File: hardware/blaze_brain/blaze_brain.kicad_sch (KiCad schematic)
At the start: 14 parts, among them J1 Conn_01x02, J3 Conn_01x30, J4 Micro_SD_Card, J5 Conn_01x03_Pin, Q2 FDN340P, U3 Teensy4.0, U4 W25N02KVZEIR

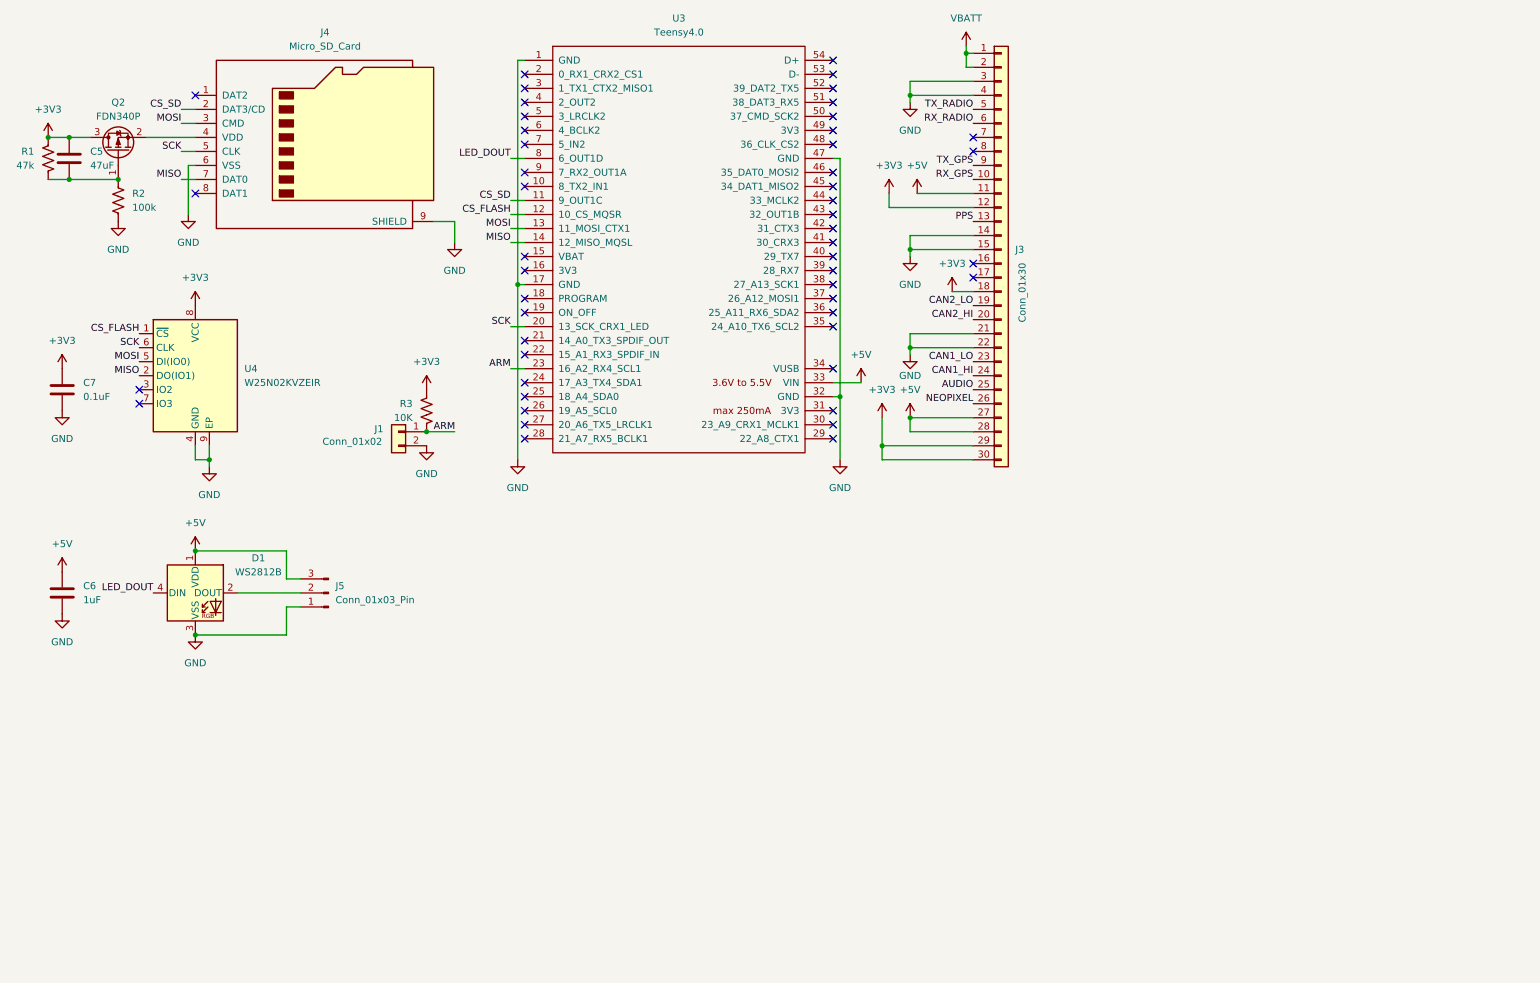
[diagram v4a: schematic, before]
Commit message: Added CAN to Blaze Brain
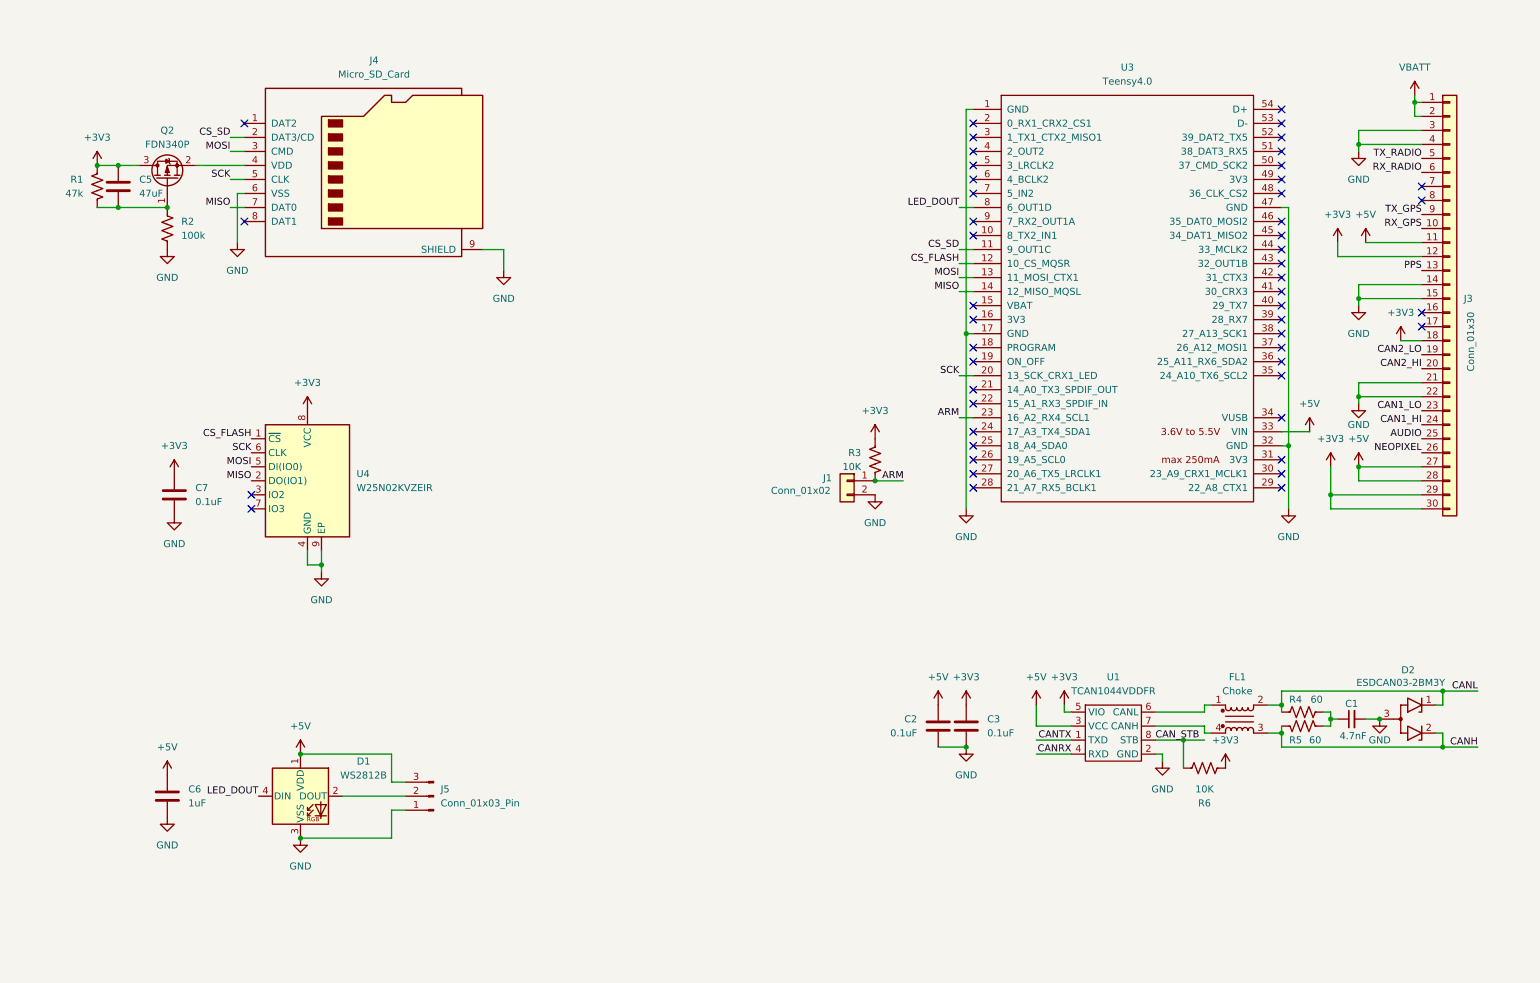
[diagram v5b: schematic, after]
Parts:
- added C1: 4.7nF, symbol Device:C_Small
- added C2, C3: 0.1uF, symbol Device:C
- added D2: ESDCAN03-2BM3Y, Package_TO_SOT_SMD:SOT-416, symbol Power_Protection:RCLAMP0582B
- added FL1: Choke, Inductor_SMD:L_CommonModeChoke_Coilcraft_0603USB, symbol Filter:Choke_Coilcraft_0603USB-142
- added R4, R5: 60, symbol Device:R_US
- added R6: 10K, symbol Device:R_US
- added U1: TCAN1044VDDFR, symbol Blaze_Lib:TCAN1044
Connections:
- net +3V3: now also C3.1, R6.2, U1.5 (VIO)
- net +5V: now also C2.1, U1.3 (VCC)
- net GND: now also C1.2, C2.2, C3.2, D2.3 (A), U1.2 (GND)
- new net: C1.1, R4.2, R5.2
- new net: FL1.1, U1.6 (CANL)
- new net: FL1.4, U1.7 (CANH)
- new net CANH: D2.2 (K2), FL1.3, R5.1
- new net CANL: D2.1 (K1), FL1.2, R4.1
- new net CANRX: U1.4 (RXD)
- new net CANTX: U1.1 (TXD)
- new net CAN_STB: R6.1, U1.8 (STB)
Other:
- moved on the sheet: C5, C6, C7, D1, J1, J3, J4, J5, Q2, R1, R2, R3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

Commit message: Connected Blaze Brain CAN
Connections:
- net CANRX: now also U3.2 (0_RX1_CRX2_CS1)
- net CANTX: now also U3.3 (1_TX1_CTX2_MISO1)
- no-connect marks 50 -> 48
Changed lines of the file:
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@@
-	)
-	(no_connect
-		(at 186.69 38.1)
 	)
 	(no_connect
@@
 	)
 	(no_connect
-		(at 186.69 35.56)
-	)
-	(no_connect
 		(at 242.57 60.96)
 	)
@@
 	(wire
 		(pts
+			(xy 184.15 35.56) (xy 186.69 35.56)
+		)
+		(stroke
+			(width 0)
+			(type default)
+		)
+	)
+	(wire
+		(pts
 			(xy 184.15 50.8) (xy 186.69 50.8)
 		)
@@
 		(pts
 			(xy 256.54 67.31) (xy 256.54 68.58)
+		)
+		(stroke
+			(width 0)
+			(type default)
+		)
+	)
+	(wire
+		(pts
+			(xy 184.15 38.1) (xy 186.69 38.1)
 		)
 		(stroke
@@
 		)
 	)
+	(label "CANTX"
+		(at 184.15 38.1 180)
+		(fields_autoplaced yes)
+		(effects
+			(font
+				(size 1.27 1.27)
+			)
+			(justify right bottom)
+		)
+	)
 	(label "RX_RADIO"
 		(at 267.97 44.45 180)
@@
 		(fields_autoplaced yes)
 		(effects
+			(font
+				(size 1.27 1.27)
+			)
+			(justify right bottom)
+		)
+	)
+	(label "CANRX"
+		(at 184.15 35.56 180)
+		(fields_autoplaced yes)
+		(effects

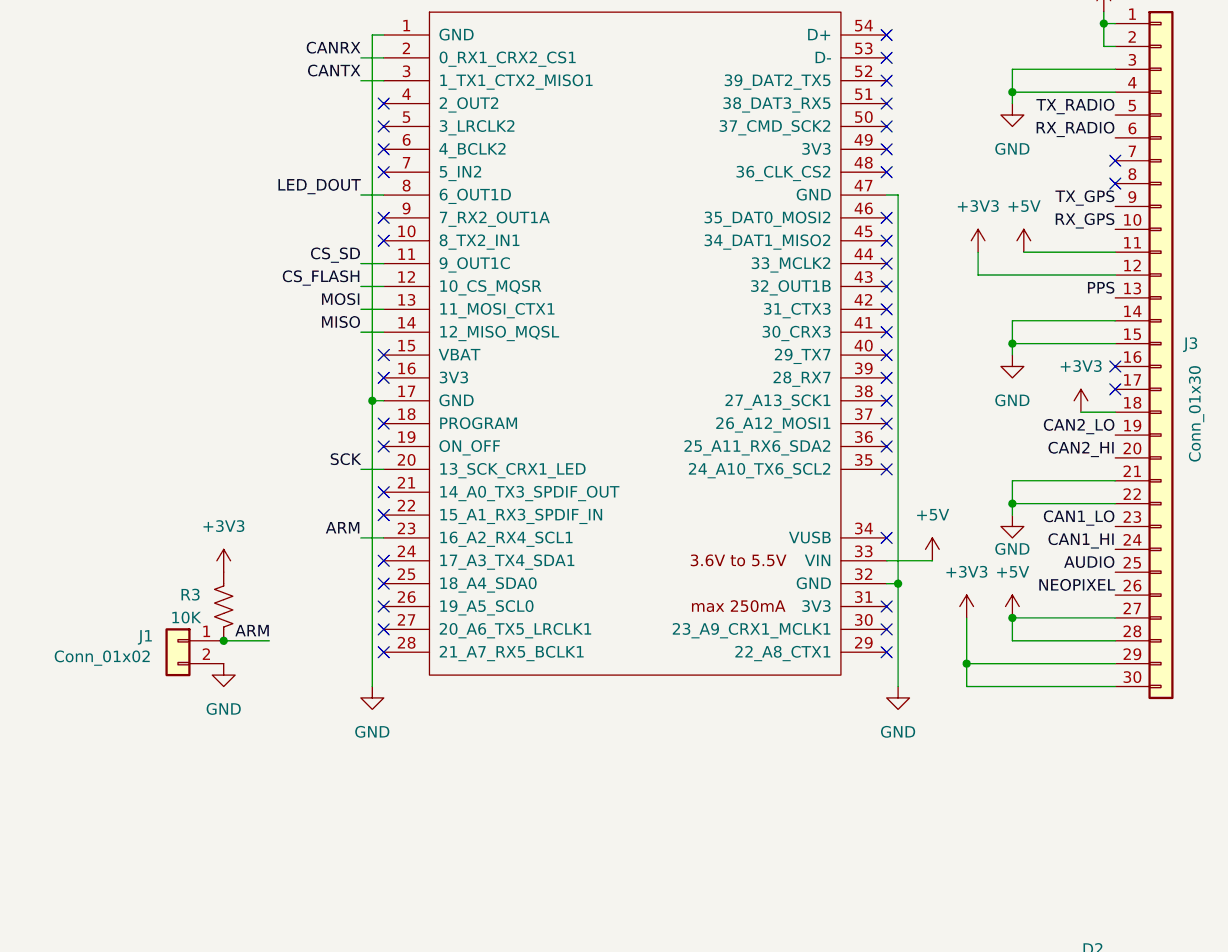
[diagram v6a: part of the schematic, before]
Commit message: Switched arm to active high and added to interconnect
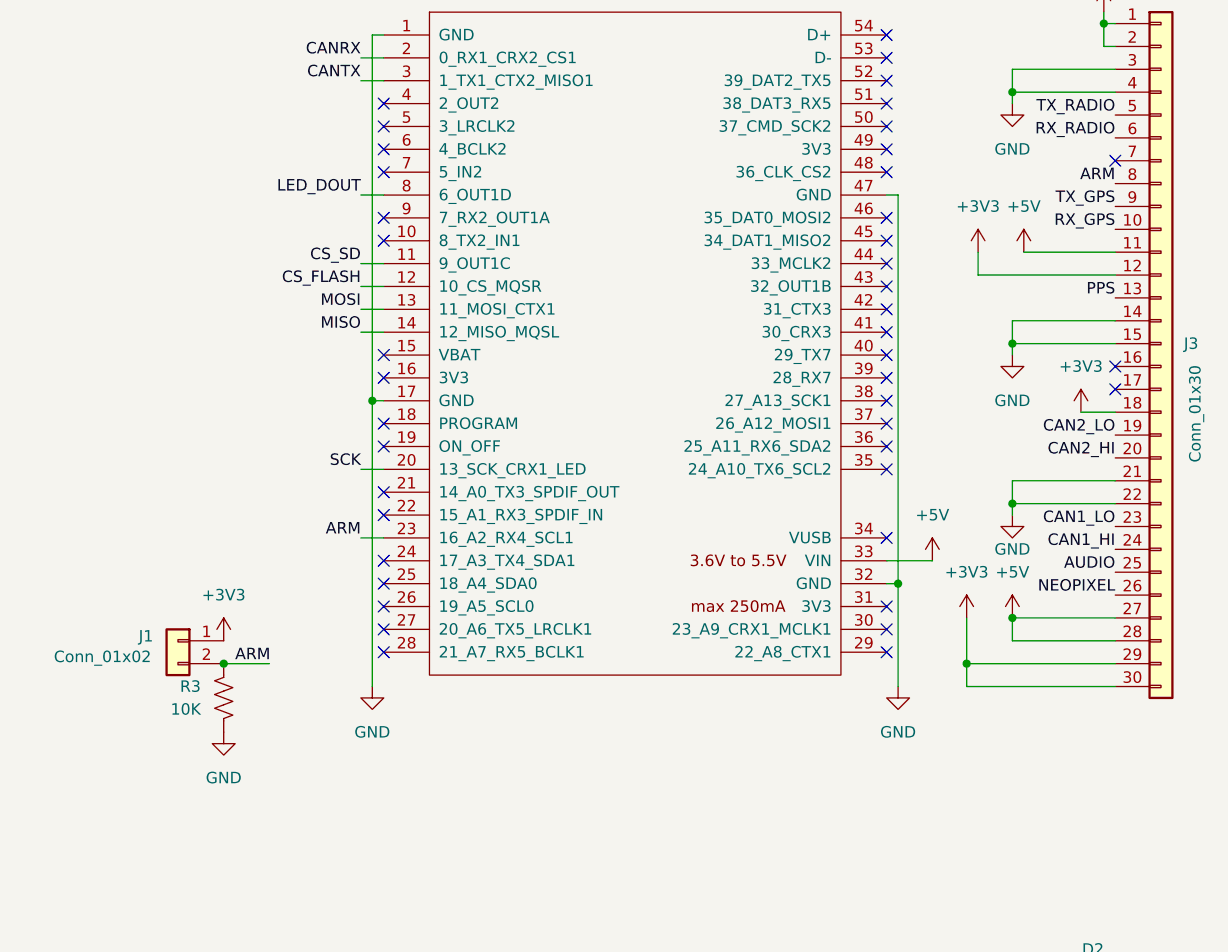
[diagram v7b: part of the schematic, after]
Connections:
- net +3V3: now also J1.1 (Pin_1); no longer R3.1
- net ARM: now also J1.2 (Pin_2), J3.8 (Pin_8), R3.1; no longer J1.1 (Pin_1), R3.2
- net GND: now also R3.2; no longer J1.2 (Pin_2)
- no-connect marks 48 -> 47

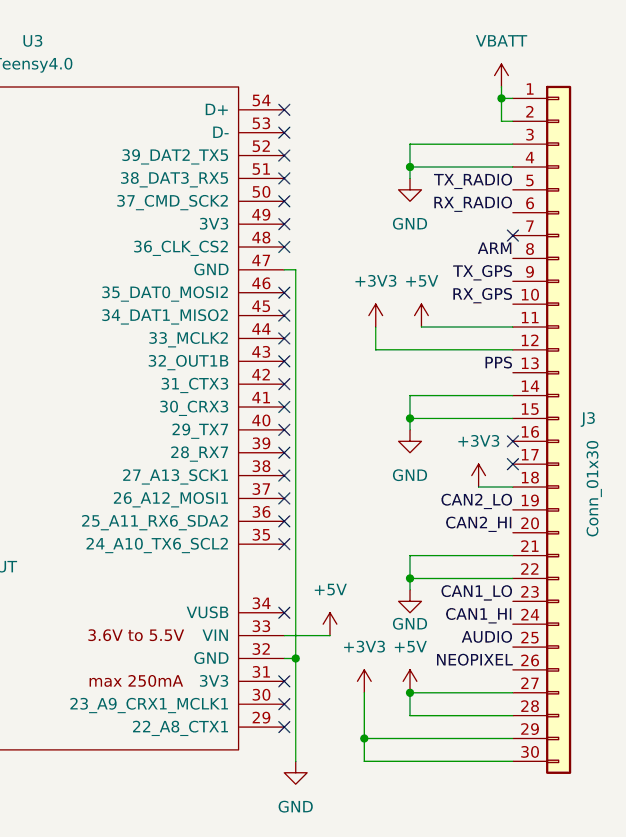
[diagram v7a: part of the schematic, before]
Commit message: Removed audio, neopixel, can2 from interconnect
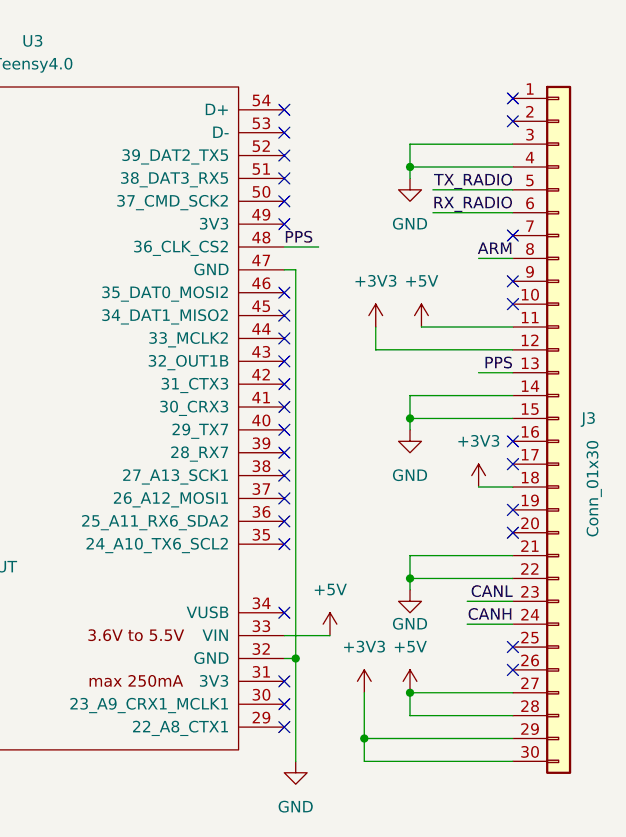
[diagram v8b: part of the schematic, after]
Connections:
- net CAN1_HI is gone; now on net CANH: J3.24 (Pin_24)
- net CAN1_LO is gone; now on net CANL: J3.23 (Pin_23)
- net PPS: now also U3.48 (36_CLK_CS2)
- net AUDIO: no longer names the net of J3.25 (Pin_25)
- net CAN2_HI: no longer names the net of J3.20 (Pin_20)
- net CAN2_LO: no longer names the net of J3.19 (Pin_19)
- net NEOPIXEL: no longer names the net of J3.26 (Pin_26)
- net RX_GPS: no longer names the net of J3.10 (Pin_10)
- net TX_GPS: no longer names the net of J3.9 (Pin_9)
- net VBATT: no longer names the net of J3.1 (Pin_1)
- net VBATT: no longer J3.2 (Pin_2)
- no-connect marks 47 -> 54
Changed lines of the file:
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@@
 	)
 	(junction
-		(at 266.7 31.75)
-		(diameter 0)
-		(color 0 0 0 0)
-	)
-	(junction
 		(at 251.46 102.87)
 		(diameter 0)
@@
 	)
 	(no_connect
+		(at 267.97 77.47)
+	)
+	(no_connect
 		(at 242.57 53.34)
 	)
@@
 	)
 	(no_connect
+		(at 267.97 95.25)
+	)
+	(no_connect
 		(at 186.69 99.06)
 	)
@@
 	)
 	(no_connect
+		(at 267.97 31.75)
+	)
+	(no_connect
 		(at 186.69 43.18)
 	)
@@
 	)
 	(no_connect
+		(at 267.97 52.07)
+	)
+	(no_connect
+		(at 267.97 54.61)
+	)
+	(no_connect
 		(at 242.57 96.52)
 	)
 	(no_connect
+		(at 267.97 34.29)
+	)
+	(no_connect
 		(at 242.57 58.42)
 	)
@@
 	)
 	(no_connect
+		(at 267.97 92.71)
+	)
+	(no_connect
 		(at 54.61 53.34)
 	)
@@
 	)
 	(no_connect
-		(at 242.57 48.26)
-	)
-	(no_connect
 		(at 186.69 55.88)
 	)
@@
 		(at 242.57 101.6)
 	)
+	(no_connect
+		(at 267.97 80.01)
+	)
 	(wire
 		(pts
@@
 	(wire
 		(pts
-			(xy 266.7 31.75) (xy 266.7 34.29)
+			(xy 262.89 87.63) (xy 267.97 87.63)
 		)
 		(stroke
@@
 	(wire
 		(pts
+			(xy 242.57 48.26) (xy 246.38 48.26)
+		)
+		(stroke
+			(width 0)
+			(type default)
+		)
+	)
+	(wire
+		(pts
 			(xy 228.6 140.97) (xy 229.87 140.97)
 		)
@@
 	(wire
 		(pts
-			(xy 266.7 30.48) (xy 266.7 31.75)
+			(xy 262.89 90.17) (xy 267.97 90.17)
 		)
 		(stroke
@@
 	(wire
 		(pts
-			(xy 266.7 31.75) (xy 267.97 31.75)
-		)
-		(stroke
-			(width 0)
-			(type default)
-		)
-	)
-	(wire
-		(pts
 			(xy 184.15 66.04) (xy 186.69 66.04)
 		)
@@
 	(wire
 		(pts
-			(xy 266.7 34.29) (xy 267.97 34.29)
-		)
-		(stroke
-			(width 0)
-			(type default)
-		)
-	)
-	(wire
-		(pts
 			(xy 184.15 88.9) (xy 186.69 88.9)
 		)
@@
 	(wire
 		(pts
+			(xy 264.16 62.23) (xy 267.97 62.23)
+		)
+		(stroke
+			(width 0)
+			(type default)
+		)
+	)
+	(wire
+		(pts
 			(xy 185.42 73.66) (xy 186.69 73.66)
 		)
@@
 	(wire
 		(pts
+			(xy 259.08 41.91) (xy 267.97 41.91)
+		)
+		(stroke
+			(width 0)
+			(type default)
+		)
+	)
+	(wire
+		(pts
 			(xy 251.46 143.51) (xy 252.73 143.51)
 		)
@@
 	(wire
 		(pts
+			(xy 264.16 49.53) (xy 267.97 49.53)
+		)
+		(stroke
+			(width 0)
+			(type default)
+		)
+	)
+	(wire
+		(pts
 			(xy 256.54 67.31) (xy 267.97 67.31)
 		)
@@
 	(wire
 		(pts
+			(xy 259.08 44.45) (xy 267.97 44.45)
+		)
+		(stroke
+			(width 0)
+			(type default)
+		)
+	)
+	(wire
+		(pts
 			(xy 256.54 82.55) (xy 267.97 82.55)
 		)
@@
 		)
 	)
-	(label "NEOPIXEL"
-		(at 267.97 95.25 180)
-		(fields_autoplaced yes)
-		(effects
-			(font
-				(size 1.27 1.27)
-			)
-			(justify right bottom)
-		)
-	)
 	(label "MOSI"
 		(at 52.07 40.64 180)
@@
 		)
 	)
-	(label "RX_GPS"
-		(at 267.97 54.61 180)
-		(fields_autoplaced yes)
-		(effects
-			(font
-				(size 1.27 1.27)
-			)
-			(justify right bottom)
-		)
-	)
-	(label "CAN2_LO"
-		(at 267.97 77.47 180)
-		(fields_autoplaced yes)
-		(effects
-			(font
-				(size 1.27 1.27)
-			)
-			(justify right bottom)
-		)
-	)
 	(label "SCK"
 		(at 52.07 45.72 180)
@@
 		)
 	)
-	(label "TX_GPS"
-		(at 267.97 52.07 180)
-		(fields_autoplaced yes)
-		(effects
-			(font
-				(size 1.27 1.27)
-			)
-			(justify right bottom)
-		)
-	)
 	(label "MISO"
 		(at 184.15 66.04 180)
@@
 		)
 	)
-	(label "AUDIO"
-		(at 267.97 92.71 180)
-		(fields_autoplaced yes)
-		(effects
-			(font
-				(size 1.27 1.27)
-			)
-			(justify right bottom)
-		)
-	)
 	(label "MOSI"
 		(at 55.88 97.79 180)
@@
 		)
 	)
-	(label "CAN2_HI"
-		(at 267.97 80.01 180)
-		(fields_autoplaced yes)
-		(effects
-			(font
-				(size 1.27 1.27)
-			)
-			(justify right bottom)
-		)
-	)
-	(label "CAN1_LO"
+	(label "CANL"
 		(at 267.97 87.63 180)
 		(fields_autoplaced yes)
@@
 		)
 	)
-	(label "CAN1_HI"
+	(label "CANH"
 		(at 267.97 90.17 180)
 		(fields_autoplaced yes)
@@
 		)
 	)
+	(label "PPS"
+		(at 242.57 48.26 0)
+		(fields_autoplaced yes)
+		(effects
+			(font
+				(size 1.27 1.27)
+			)
+			(justify left bottom)
+		)
+	)
 	(symbol
 		(lib_id "Device:R_US")
@@
 					(unit 1)
 				)
-			)
-		)
-	)
-	(symbol
-		(lib_id "power:+5V")
-		(at 266.7 30.48 0)
-		(unit 1)
-		(exclude_from_sim no)
-		(in_bom yes)
-		(on_board yes)
-		(dnp no)
-		(fields_autoplaced yes)
-		(property "Reference" "#PWR01"
-			(at 266.7 34.29 0)
-			(effects
-				(font
-					(size 1.27 1.27)
-				)
-				(hide yes)
-			)
-		)
-		(property "Value" "VBATT"
-			(at 266.7 25.4 0)
-			(effects
-				(font
-					(size 1.27 1.27)
-				)
-			)
-		)
-		(property "Footprint" ""
-			(at 266.7 30.48 0)
-			(effects
-				(font
-					(size 1.27 1.27)
-				)
-				(hide yes)
-			)
-		)
-		(property "Datasheet" ""
-			(at 266.7 30.48 0)
-			(effects
-				(font
-					(size 1.27 1.27)
-				)
-				(hide yes)
-			)
-		)
-		(property "Description" "Power symbol creates a global label with name \"+5V\""
-			(at 266.7 30.48 0)
-			(effects
-				(font
-					(size 1.27 1.27)
-				)
-				(hide yes)
-			)
-		)
-		(pin "1"
-		)
-		(instances
-			(project "blaze_brain"
-				(path "/d96f300b-87d4-4b9f-96ad-2ce544b71732"
-					(reference "#PWR01")
-					(unit 1)
-				)
